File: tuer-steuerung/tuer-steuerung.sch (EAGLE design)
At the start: 47 parts, among them IC1 L6203, IC2 MEGA8-P, Q1 16Mhz, T1 BC337, T2 BC337, X1 ENDSTOP1, X2 ENDSTOP2, X3 DOORSTATE, X4 LOCKSTATE, X5 MOTOR, X6 NERDSTERN

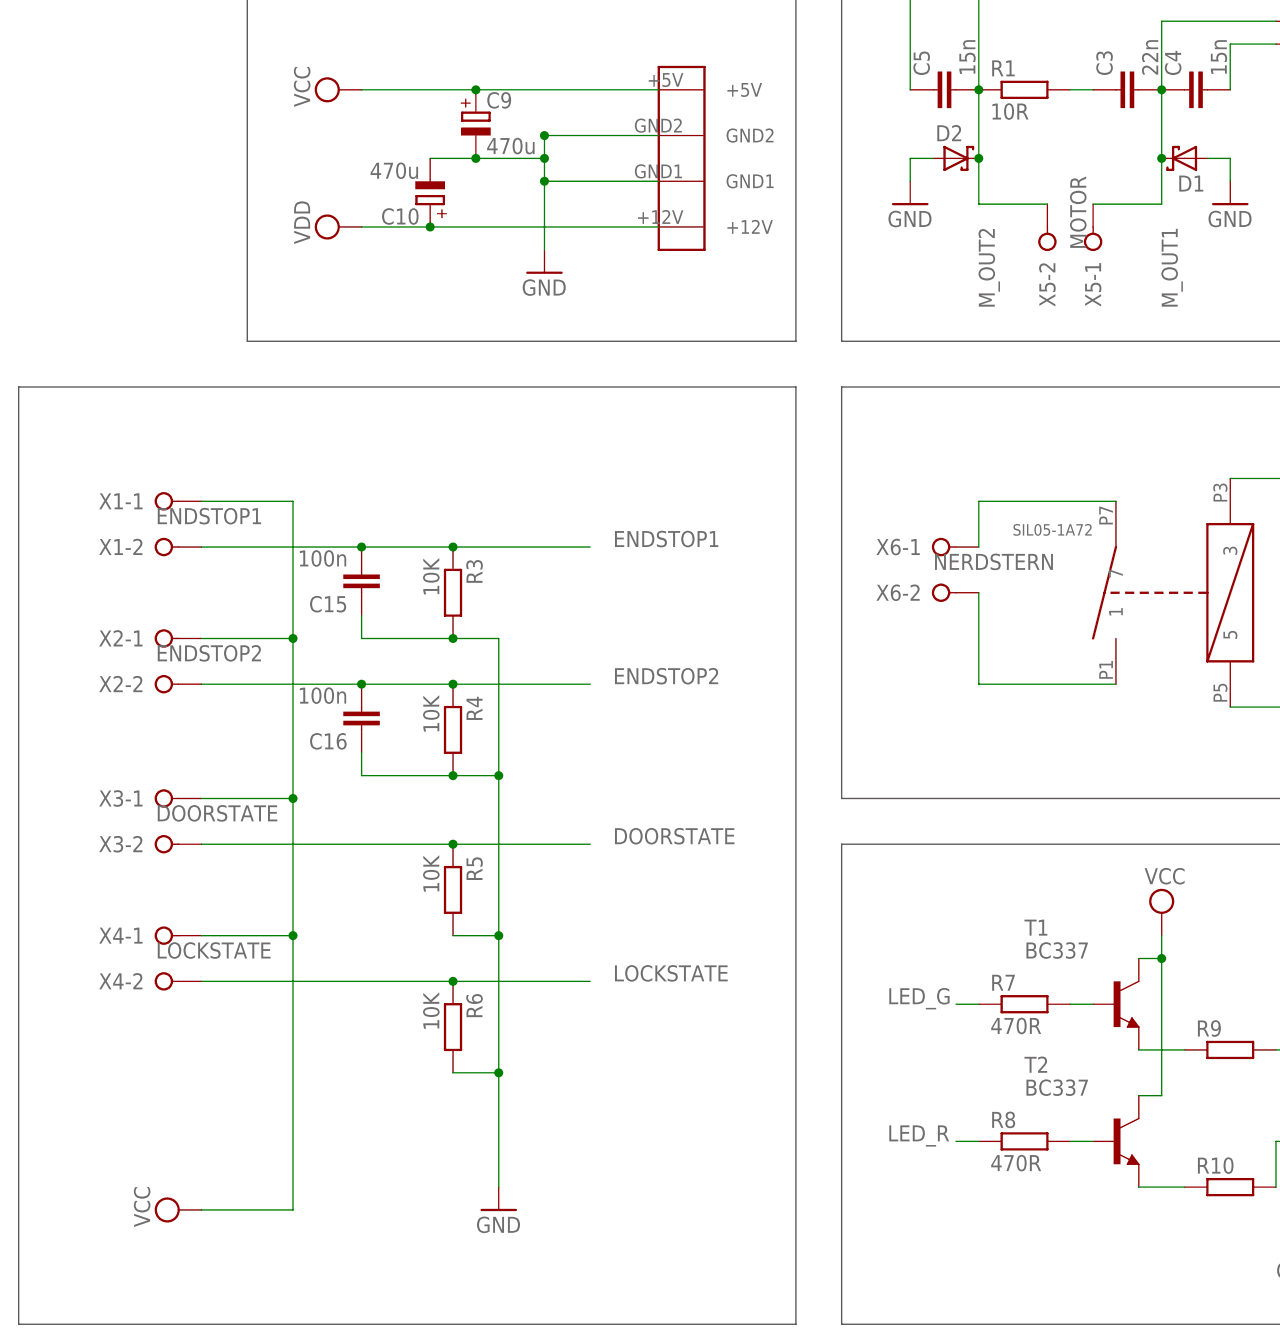
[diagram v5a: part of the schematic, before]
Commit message: Anschlussklemmen angepasst
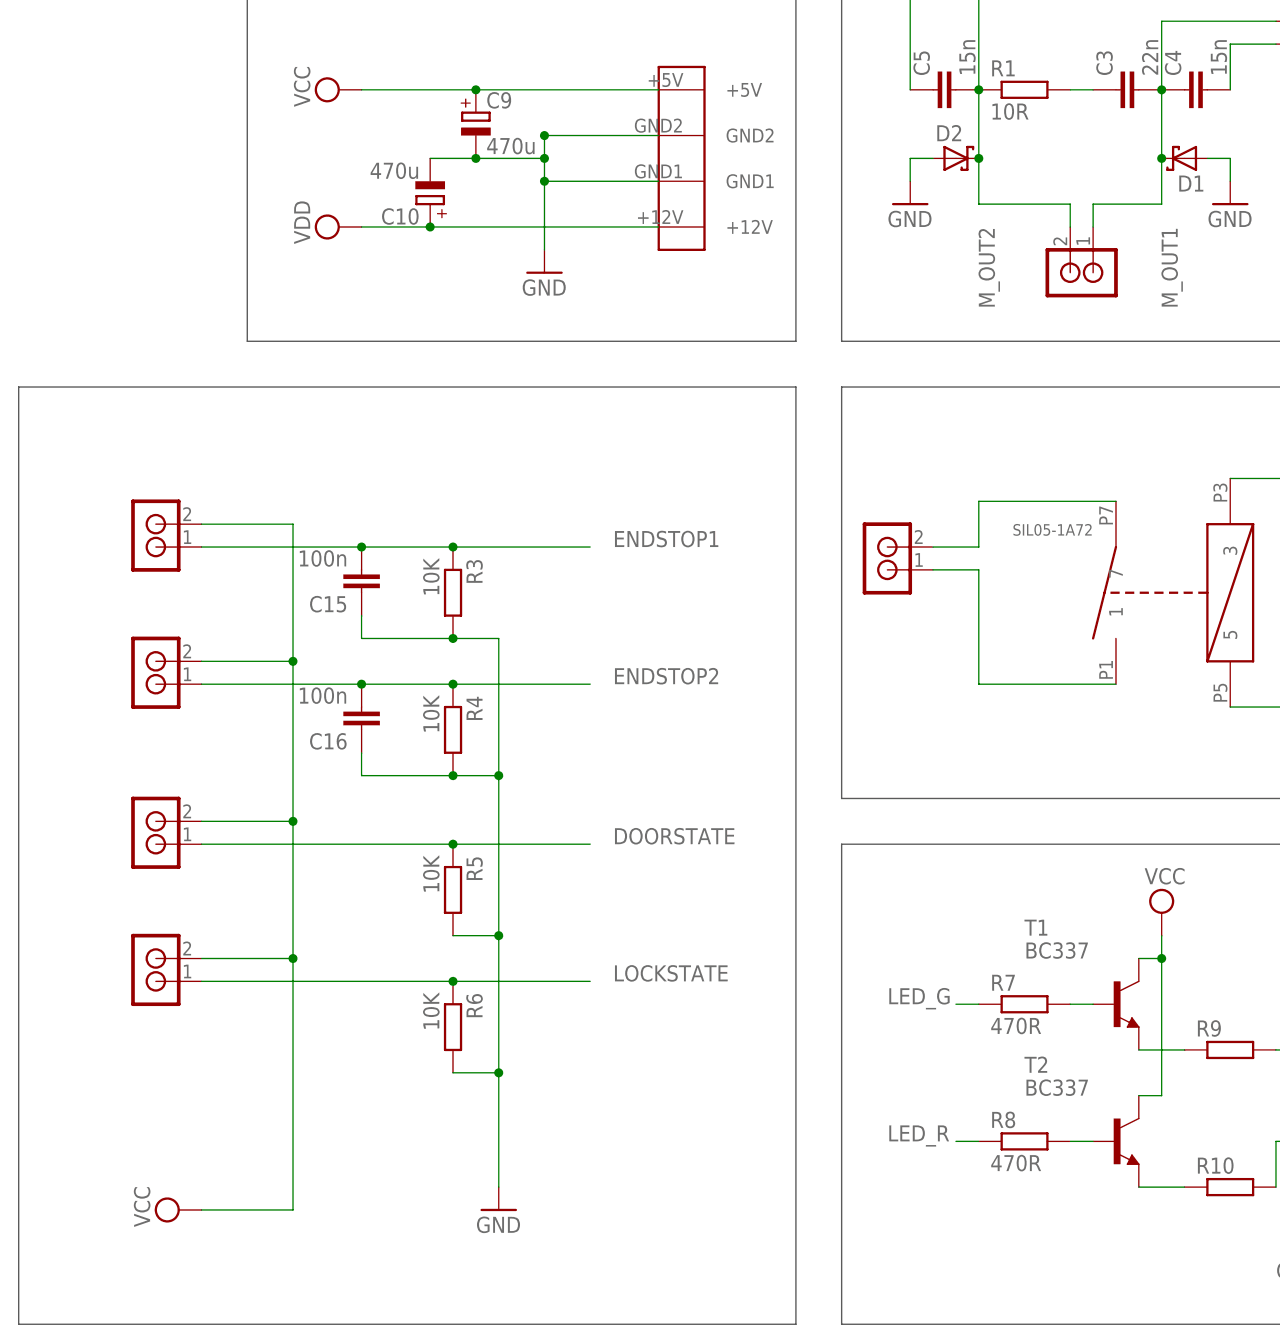
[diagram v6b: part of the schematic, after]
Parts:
- removed X1: ENDSTOP1, con-wago-508:W237-02P
- removed X2: ENDSTOP2, con-wago-508:W237-02P
- removed X3: DOORSTATE, con-wago-508:W237-02P
- removed X4: LOCKSTATE, con-wago-508:W237-02P
- removed X5: MOTOR, con-wago-508:W237-02P
- removed X6: NERDSTERN, con-wago-508:W237-02P
- added DOORSTATE, ENDSTOP1, ENDSTOP2, LOCKSTATE, MOTOR, NERDSTERN: RIACON_101_2, n39:RIACON_101_2
- C6, C7: device resistor:C-EUC0805K -> resistor:C-EU050-025X075
- R3, R4, R5, R6: device resistor:R-EU_R0805W -> resistor:R-EU_0204/5
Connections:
- net DOORSTATE: now also DOORSTATE.1; no longer X3-2.KL
- net ENDSTOP1: now also ENDSTOP1.1; no longer X1-2.KL
- net ENDSTOP2: now also ENDSTOP2.1; no longer X2-2.KL
- net LOCKSTATE: now also LOCKSTATE.1; no longer X4-2.KL
- net M_OUT1: now also MOTOR.1; no longer X5-1.KL
- net M_OUT2: now also MOTOR.2; no longer X5-2.KL
- net N$4: now also NERDSTERN.2; no longer X6-1.KL
- net N$5: now also NERDSTERN.1; no longer X6-2.KL
- net VCC: now also DOORSTATE.2, ENDSTOP1.2, ENDSTOP2.2, LOCKSTATE.2; no longer X1-1.KL, X2-1.KL, X3-1.KL, X4-1.KL

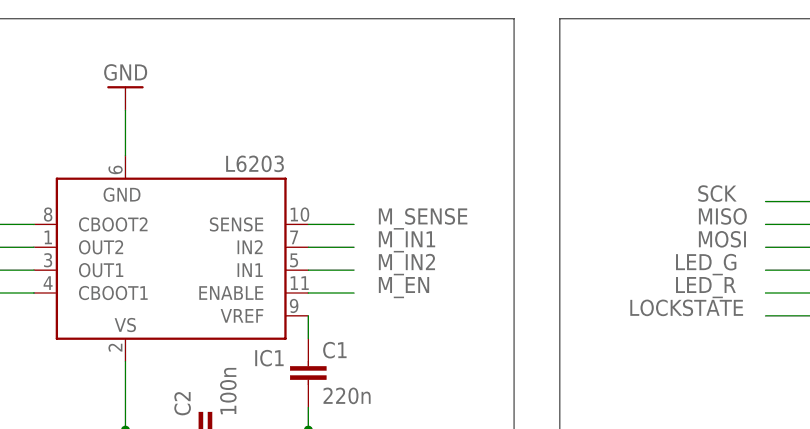
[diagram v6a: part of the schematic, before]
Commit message: SENSE -> GND
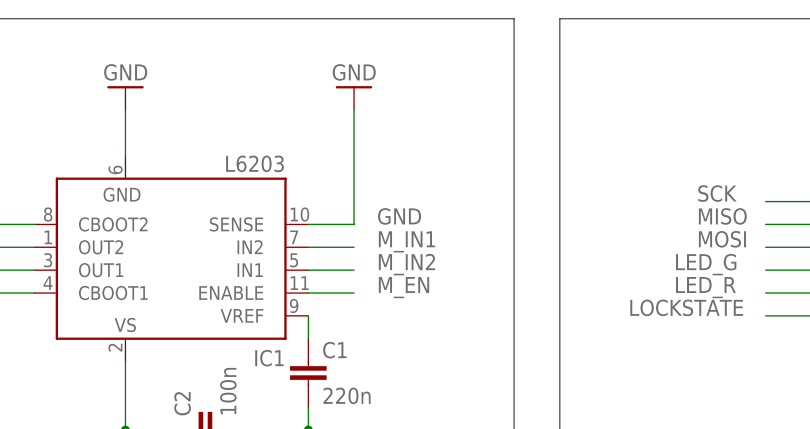
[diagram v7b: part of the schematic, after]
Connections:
- removed net M_SENSE: IC1.SENSE
- net GND: now also IC1.SENSE
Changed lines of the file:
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@@
 <grid distance="0.1" unitdist="inch" unit="inch" style="lines" multiple="1" display="no" altdistance="0.01" altunitdist="inch" altunit="inch"/>
 <layers>
-<layer number="1" name="Top" color="4" fill="1" visible="yes" active="no"/>
-<layer number="16" name="Bottom" color="1" fill="1" visible="yes" active="no"/>
-<layer number="17" name="Pads" color="2" fill="1" visible="yes" active="no"/>
-<layer number="18" name="Vias" color="2" fill="1" visible="yes" active="no"/>
-<layer number="19" name="Unrouted" color="6" fill="1" visible="yes" active="no"/>
-<layer number="20" name="Dimension" color="15" fill="1" visible="yes" active="no"/>
-<layer number="21" name="tPlace" color="7" fill="1" visible="yes" active="no"/>
-<layer number="22" name="bPlace" color="7" fill="1" visible="yes" active="no"/>
-<layer number="23" name="tOrigins" color="15" fill="1" visible="yes" active="no"/>
-<layer number="24" name="bOrigins" color="15" fill="1" visible="yes" active="no"/>
-<layer number="25" name="tNames" color="7" fill="1" visible="yes" active="no"/>
-<layer number="26" name="bNames" color="7" fill="1" visible="yes" active="no"/>
-<layer number="27" name="tValues" color="7" fill="1" visible="yes" active="no"/>
-<layer number="28" name="bValues" color="7" fill="1" visible="yes" active="no"/>
+<layer number="1" name="Top" color="4" fill="1" visible="no" active="no"/>
+<layer number="16" name="Bottom" color="1" fill="1" visible="no" active="no"/>
+<layer number="17" name="Pads" color="2" fill="1" visible="no" active="no"/>
+<layer number="18" name="Vias" color="2" fill="1" visible="no" active="no"/>
+<layer number="19" name="Unrouted" color="6" fill="1" visible="no" active="no"/>
+<layer number="20" name="Dimension" color="15" fill="1" visible="no" active="no"/>
+<layer number="21" name="tPlace" color="7" fill="1" visible="no" active="no"/>
+<layer number="22" name="bPlace" color="7" fill="1" visible="no" active="no"/>
+<layer number="23" name="tOrigins" color="15" fill="1" visible="no" active="no"/>
+<layer number="24" name="bOrigins" color="15" fill="1" visible="no" active="no"/>
+<layer number="25" name="tNames" color="7" fill="1" visible="no" active="no"/>
+<layer number="26" name="bNames" color="7" fill="1" visible="no" active="no"/>
+<layer number="27" name="tValues" color="7" fill="1" visible="no" active="no"/>
+<layer number="28" name="bValues" color="7" fill="1" visible="no" active="no"/>
 <layer number="29" name="tStop" color="7" fill="3" visible="no" active="no"/>
 <layer number="30" name="bStop" color="7" fill="6" visible="no" active="no"/>
@@
 <layer number="35" name="tGlue" color="7" fill="4" visible="no" active="no"/>
 <layer number="36" name="bGlue" color="7" fill="5" visible="no" active="no"/>
-<layer number="37" name="tTest" color="7" fill="1" visible="yes" active="no"/>
-<layer number="38" name="bTest" color="7" fill="1" visible="yes" active="no"/>
+<layer number="37" name="tTest" color="7" fill="1" visible="no" active="no"/>
+<layer number="38" name="bTest" color="7" fill="1" visible="no" active="no"/>
 <layer number="39" name="tKeepout" color="4" fill="11" visible="no" active="no"/>
 <layer number="40" name="bKeepout" color="1" fill="11" visible="no" active="no"/>
@@
 <layer number="44" name="Drills" color="7" fill="1" visible="no" active="no"/>
 <layer number="45" name="Holes" color="7" fill="1" visible="no" active="no"/>
-<layer number="46" name="Milling" color="3" fill="1" visible="yes" active="no"/>
-<layer number="47" name="Measures" color="7" fill="1" visible="yes" active="no"/>
-<layer number="48" name="Document" color="7" fill="1" visible="yes" active="no"/>
-<layer number="49" name="Reference" color="7" fill="1" visible="yes" active="no"/>
-<layer number="50" name="dxf" color="7" fill="1" visible="yes" active="no"/>
-<layer number="51" name="tDocu" color="7" fill="1" visible="yes" active="no"/>
-<layer number="52" name="bDocu" color="7" fill="1" visible="yes" active="no"/>
+<layer number="46" name="Milling" color="3" fill="1" visible="no" active="no"/>
+<layer number="47" name="Measures" color="7" fill="1" visible="no" active="no"/>
+<layer number="48" name="Document" color="7" fill="1" visible="no" active="no"/>
+<layer number="49" name="Reference" color="7" fill="1" visible="no" active="no"/>
+<layer number="50" name="dxf" color="7" fill="1" visible="no" active="no"/>
+<layer number="51" name="tDocu" color="7" fill="1" visible="no" active="no"/>
+<layer number="52" name="bDocu" color="7" fill="1" visible="no" active="no"/>
 <layer number="91" name="Nets" color="2" fill="1" visible="yes" active="yes"/>
 <layer number="92" name="Busses" color="1" fill="1" visible="yes" active="yes"/>
@@
 <part name="MOTOR" library="n39" deviceset="RIACON_101_2" device=""/>
 <part name="NERDSTERN" library="n39" deviceset="RIACON_101_2" device=""/>
+<part name="GND8" library="supply1" deviceset="GND" device=""/>
 </parts>
 <sheets>
@@
 <instance part="MOTOR" gate="G$1" x="15.24" y="15.24" rot="R270"/>
 <instance part="NERDSTERN" gate="G$1" x="-7.62" y="-17.78" rot="R180"/>
+<instance part="GND8" gate="1" x="71.12" y="63.5" rot="R180"/>
 </instances>
 <busses>
@@
 <junction x="203.2" y="5.08"/>
 </segment>
+<segment>
+<pinref part="IC1" gate="G$1" pin="SENSE"/>
+<wire x1="66.04" y1="48.26" x2="71.12" y2="48.26" width="0.1524" layer="91"/>
+<label x="73.66" y="48.26" size="1.778" layer="95"/>
+<pinref part="GND8" gate="1" pin="GND"/>
+<wire x1="71.12" y1="48.26" x2="71.12" y2="60.96" width="0.1524" layer="91"/>
+</segment>
 </net>
 <net name="N$1" class="0">
@@
 </segment>
 </net>
-<net name="M_SENSE" class="0">
-<segment>
-<pinref part="IC1" gate="G$1" pin="SENSE"/>
-<wire x1="66.04" y1="48.26" x2="71.12" y2="48.26" width="0.1524" layer="91"/>
-<label x="73.66" y="48.26" size="1.778" layer="95"/>
-</segment>
-</net>
